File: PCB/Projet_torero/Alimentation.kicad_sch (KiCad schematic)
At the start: 10 parts, among them IC1 MP1475SGJ-P, J2 Conn_01x02

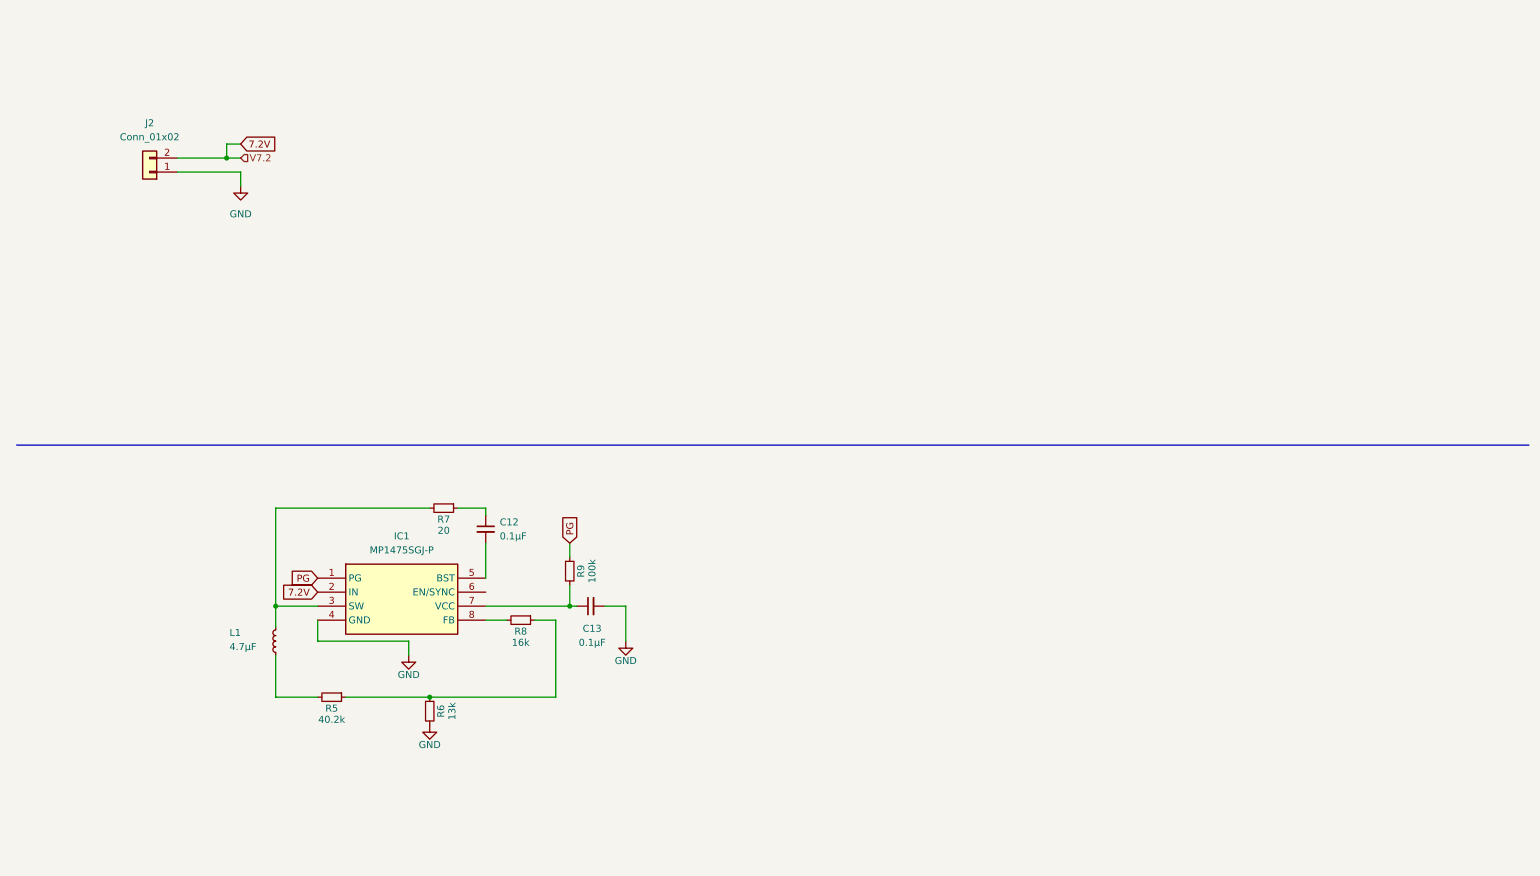
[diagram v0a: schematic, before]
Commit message: Mis à jour, manque l'interupteur ON/OFF
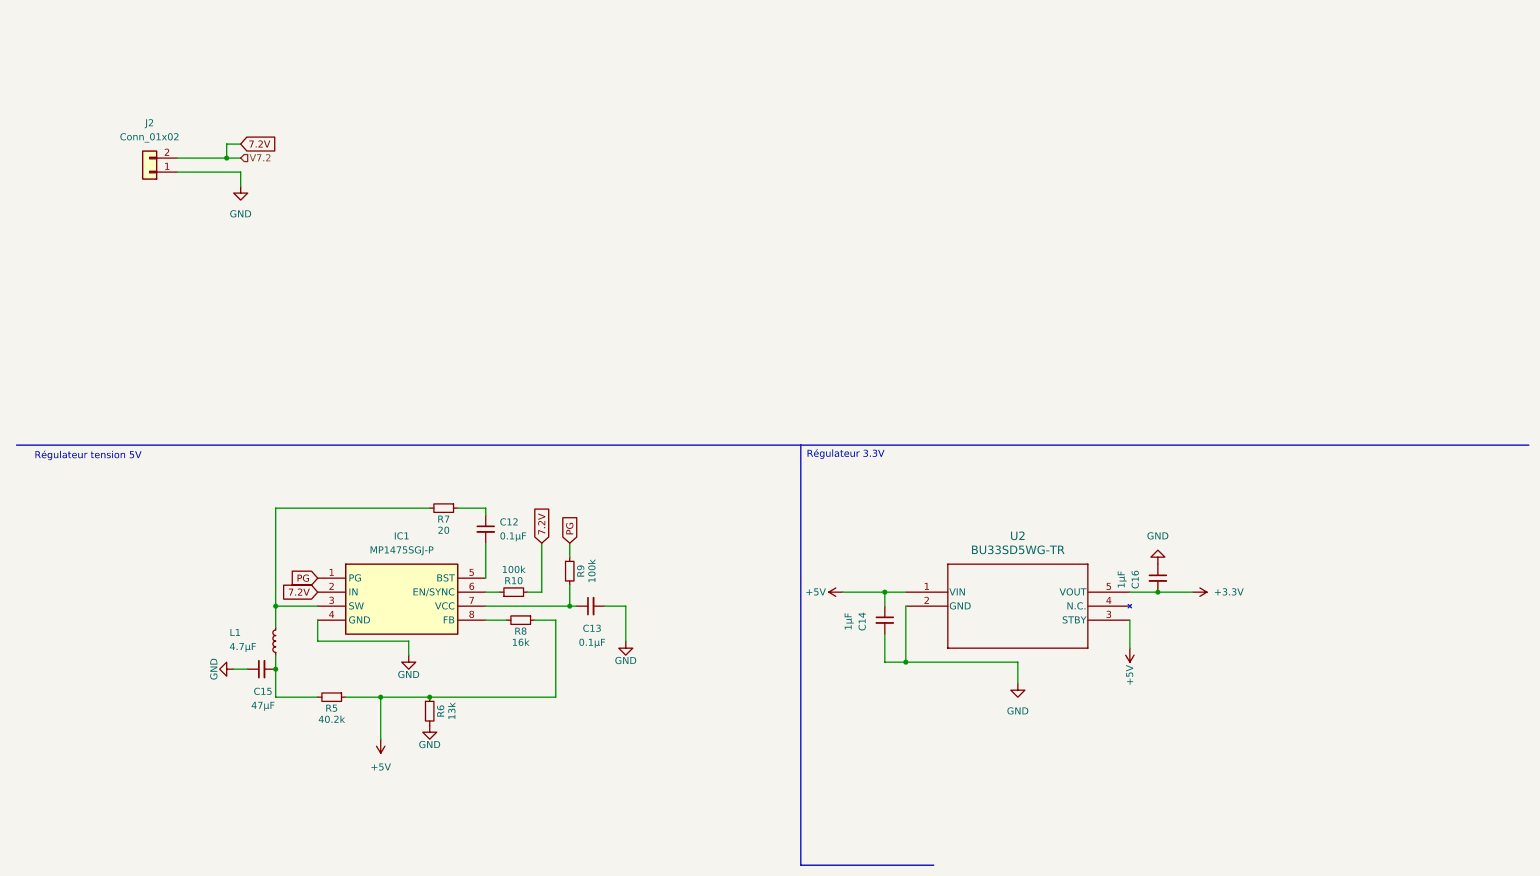
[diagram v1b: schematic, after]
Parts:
- added C14, C16: 1µF, symbol Device:C_Small
- added C15: 47µF, symbol Device:C_Small
- added R10: 100k, symbol Device:R_Small
- added U2: BU33SD5WG-TR, SSOP5_ROM, symbol 2024-10-01_06-18-21:BU33SD5WG-TR
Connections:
- net 7.2V: now also R10.2
- net GND: now also C14.2, C15.1, C16.1, U2.2 (GND)
- net at IC1.6 (EN/SYNC): now also R10.1
- net +5V: now reaches R5.1, R6.1, R8.1
- net +5V: now also C14.1, U2.1 (VIN), U2.3 (STBY)
- net at L1.1, R5.2: now also C15.2
- new net +3.3V: C16.2, U2.5 (VOUT)
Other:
- note added: "Régulateur 3.3V"
- note added: "Régulateur tension 5V"

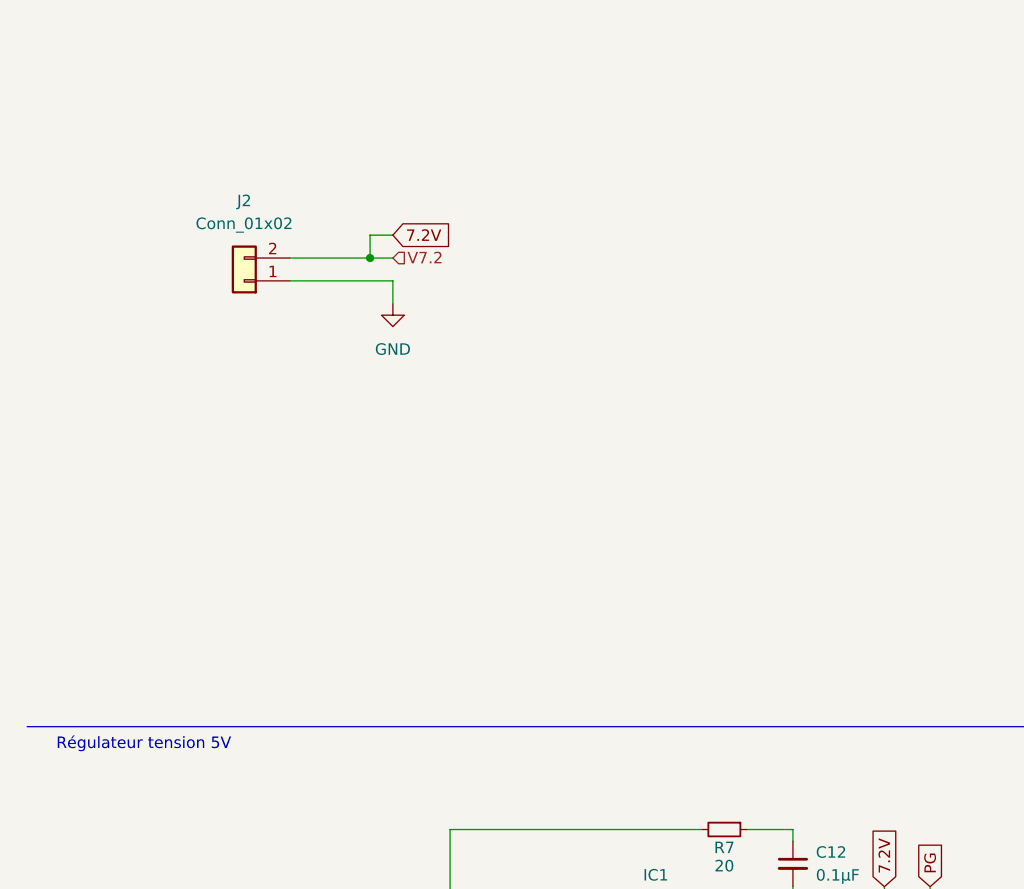
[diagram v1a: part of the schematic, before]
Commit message: Rajout interupteur ON/OFF
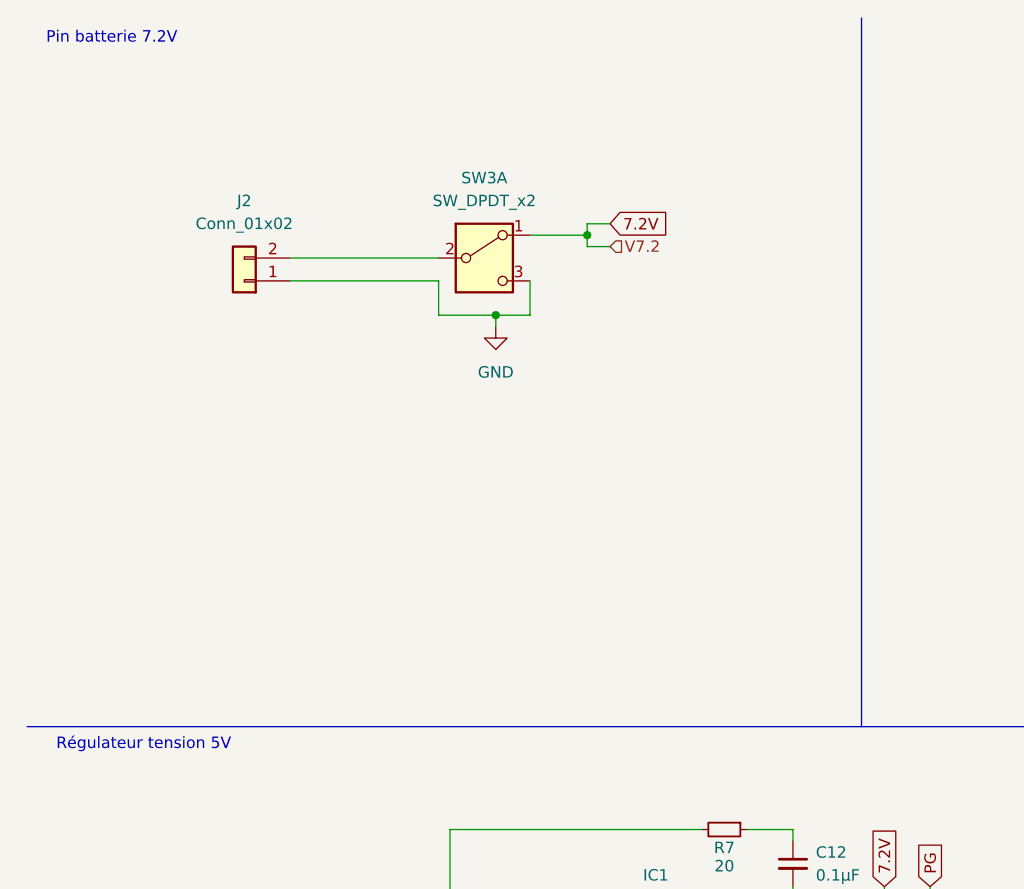
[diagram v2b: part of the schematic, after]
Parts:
- added SW3: SW_DPDT_x2, symbol Switch:SW_DPDT_x2
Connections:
- net 7.2V: now also SW3.1 (A); no longer J2.2 (Pin_2)
- net GND: now also SW3.3 (C)
- new net: J2.2 (Pin_2), SW3.2 (B)
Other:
- note added: "Pin batterie 7.2V"
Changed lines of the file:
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@@
+	)
+	(junction
+		(at 63.5 44.45)
+		(diameter 0)
+		(color 0 0 0 0)
 	)
 	(junction
@@
 	)
 	(junction
-		(at 49.53 38.1)
-		(diameter 0)
-		(color 0 0 0 0)
-	)
-	(junction
 		(at 218.44 116.84)
 		(diameter 0)
@@
 		(color 0 0 0 0)
 	)
+	(junction
+		(at 73.66 35.56)
+		(diameter 0)
+		(color 0 0 0 0)
+	)
 	(wire
 		(pts
@@
 		)
 	)
+	(polyline
+		(pts
+			(xy 104.14 11.43) (xy 104.14 90.17)
+		)
+		(stroke
+			(width 0)
+			(type default)
+		)
+	)
 	(wire
 		(pts
@@
 	(wire
 		(pts
-			(xy 52.07 35.56) (xy 49.53 35.56)
-		)
-		(stroke
-			(width 0)
-			(type default)
-		)
-	)
-	(wire
-		(pts
-			(xy 40.64 40.64) (xy 52.07 40.64)
+			(xy 76.2 34.29) (xy 73.66 34.29)
 		)
 		(stroke
@@
 	(wire
 		(pts
+			(xy 57.15 44.45) (xy 63.5 44.45)
+		)
+		(stroke
+			(width 0)
+			(type default)
+		)
+	)
+	(wire
+		(pts
 			(xy 96.52 107.95) (xy 96.52 114.3)
 		)
@@
 	(wire
 		(pts
-			(xy 52.07 40.64) (xy 52.07 43.18)
+			(xy 57.15 40.64) (xy 57.15 44.45)
 		)
 		(stroke
@@
 	(wire
 		(pts
+			(xy 57.15 40.64) (xy 40.64 40.64)
+		)
+		(stroke
+			(width 0)
+			(type default)
+		)
+	)
+	(wire
+		(pts
+			(xy 67.31 40.64) (xy 67.31 44.45)
+		)
+		(stroke
+			(width 0)
+			(type default)
+		)
+	)
+	(wire
+		(pts
 			(xy 58.42 128.27) (xy 58.42 130.81)
 		)
@@
 	(wire
 		(pts
-			(xy 49.53 35.56) (xy 49.53 38.1)
+			(xy 73.66 34.29) (xy 73.66 35.56)
+		)
+		(stroke
+			(width 0)
+			(type default)
+		)
+	)
+	(wire
+		(pts
+			(xy 63.5 44.45) (xy 63.5 45.72)
 		)
 		(stroke
@@
 	(wire
 		(pts
+			(xy 73.66 35.56) (xy 73.66 36.83)
+		)
+		(stroke
+			(width 0)
+			(type default)
+		)
+	)
+	(wire
+		(pts
 			(xy 66.04 121.92) (xy 66.04 125.73)
 		)
@@
 	(wire
 		(pts
-			(xy 40.64 38.1) (xy 49.53 38.1)
-		)
-		(stroke
-			(width 0)
-			(type default)
-		)
-	)
-	(wire
-		(pts
 			(xy 58.42 135.89) (xy 66.04 135.89)
 		)
@@
 	(wire
 		(pts
+			(xy 67.31 35.56) (xy 73.66 35.56)
+		)
+		(stroke
+			(width 0)
+			(type default)
+		)
+	)
+	(wire
+		(pts
 			(xy 71.12 135.89) (xy 77.47 135.89)
 		)
@@
 	(wire
 		(pts
-			(xy 49.53 38.1) (xy 52.07 38.1)
+			(xy 73.66 36.83) (xy 76.2 36.83)
 		)
 		(stroke
@@
 	(wire
 		(pts
+			(xy 40.64 38.1) (xy 57.15 38.1)
+		)
+		(stroke
+			(width 0)
+			(type default)
+		)
+	)
+	(wire
+		(pts
 			(xy 111.76 110.49) (xy 111.76 107.95)
 		)
@@
 			(width 0)
 			(type default)
+		)
+	)
+	(wire
+		(pts
+			(xy 67.31 44.45) (xy 63.5 44.45)
+		)
+		(stroke
+			(width 0)
+			(type default)
+		)
+	)
+	(text "Pin batterie 7.2V"
+		(exclude_from_sim no)
+		(at 20.828 13.716 0)
+		(effects
+			(font
+				(size 1.27 1.27)
+			)
 		)
 	)
@@
 	(global_label "7.2V"
 		(shape input)
-		(at 52.07 35.56 0)
+		(at 76.2 34.29 0)
 		(fields_autoplaced yes)
 		(effects
@@
 		)
 		(property "Intersheetrefs" "${INTERSHEET_REFS}"
-			(at 59.1676 35.56 0)
+			(at 83.2976 34.29 0)
 			(effects
 				(font
@@
 	(hierarchical_label "V7.2"
 		(shape input)
-		(at 52.07 38.1 0)
+		(at 76.2 36.83 0)
 		(fields_autoplaced yes)
 		(effects
@@
 	)
 	(symbol
+		(lib_id "Switch:SW_DPDT_x2")
+		(at 62.23 38.1 0)
+		(unit 1)
+		(exclude_from_sim no)
+		(in_bom yes)
+		(on_board yes)
+		(dnp no)
+		(fields_autoplaced yes)
+		(property "Reference" "SW3"
+			(at 62.23 29.21 0)
+			(effects
+				(font
+					(size 1.27 1.27)
+				)
+			)
+		)
+		(property "Value" "SW_DPDT_x2"
+			(at 62.23 31.75 0)
+			(effects
+				(font
+					(size 1.27 1.27)
+				)
+			)
+		)
+		(property "Footprint" ""
+			(at 62.23 38.1 0)
+			(effects
+				(font
+					(size 1.27 1.27)
+				)
+				(hide yes)
+			)
+		)
+		(property "Datasheet" "~"
+			(at 62.23 38.1 0)
+			(effects
+				(font
+					(size 1.27 1.27)
+				)
+				(hide yes)
+			)
+		)
+		(property "Description" "Switch, dual pole double throw, separate symbols"
+			(at 62.23 38.1 0)
+			(effects
+				(font
+					(size 1.27 1.27)
+				)
+				(hide yes)
+			)
+		)
+		(pin "1"
+		)
+		(pin "2"
+		)
+		(pin "3"
+		)
+		(pin "4"
+		)
+		(pin "5"
+		)
+		(pin "6"
+		)
+		(instances
+			(project ""
+				(path "/04e1eb47-a2c4-462b-bef7-377d9515a2c0/b3b2826c-2e3c-42fe-bcd6-22fcd6249c25"
+					(reference "SW3")
+					(unit 1)
+				)
+			)
+		)
+	)
+	(symbol
 		(lib_id "power:GND")
 		(at 218.44 111.76 180)
@@
 	(symbol
 		(lib_id "power:GND")
-		(at 52.07 43.18 0)
+		(at 63.5 45.72 0)
 		(unit 1)
 		(exclude_from_sim no)
@@
 		(fields_autoplaced yes)
 		(property "Reference" "#PWR021"
-			(at 52.07 49.53 0)
+			(at 63.5 52.07 0)
 			(effects
 				(font
@@
 		)
 		(property "Value" "GND"
-			(at 52.07 48.26 0)
+			(at 63.5 50.8 0)
 			(effects
 				(font
@@
 		)
 		(property "Footprint" ""
-			(at 52.07 43.18 0)
+			(at 63.5 45.72 0)
 			(effects
 				(font
@@
 		)
 		(property "Datasheet" ""
-			(at 52.07 43.18 0)
+			(at 63.5 45.72 0)
 			(effects
 				(font
@@
 		)
 		(property "Description" "Power symbol creates a global label with name \"GND\" , ground"
-			(at 52.07 43.18 0)
-			(effects
-				(font
+			(at 63.5 45.72 0)
+			(effects
+				(font
